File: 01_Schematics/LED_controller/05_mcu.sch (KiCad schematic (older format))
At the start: 28 parts, among them J48 PLS-4, U8 STM32F107RCTx, Y1 25 MHz

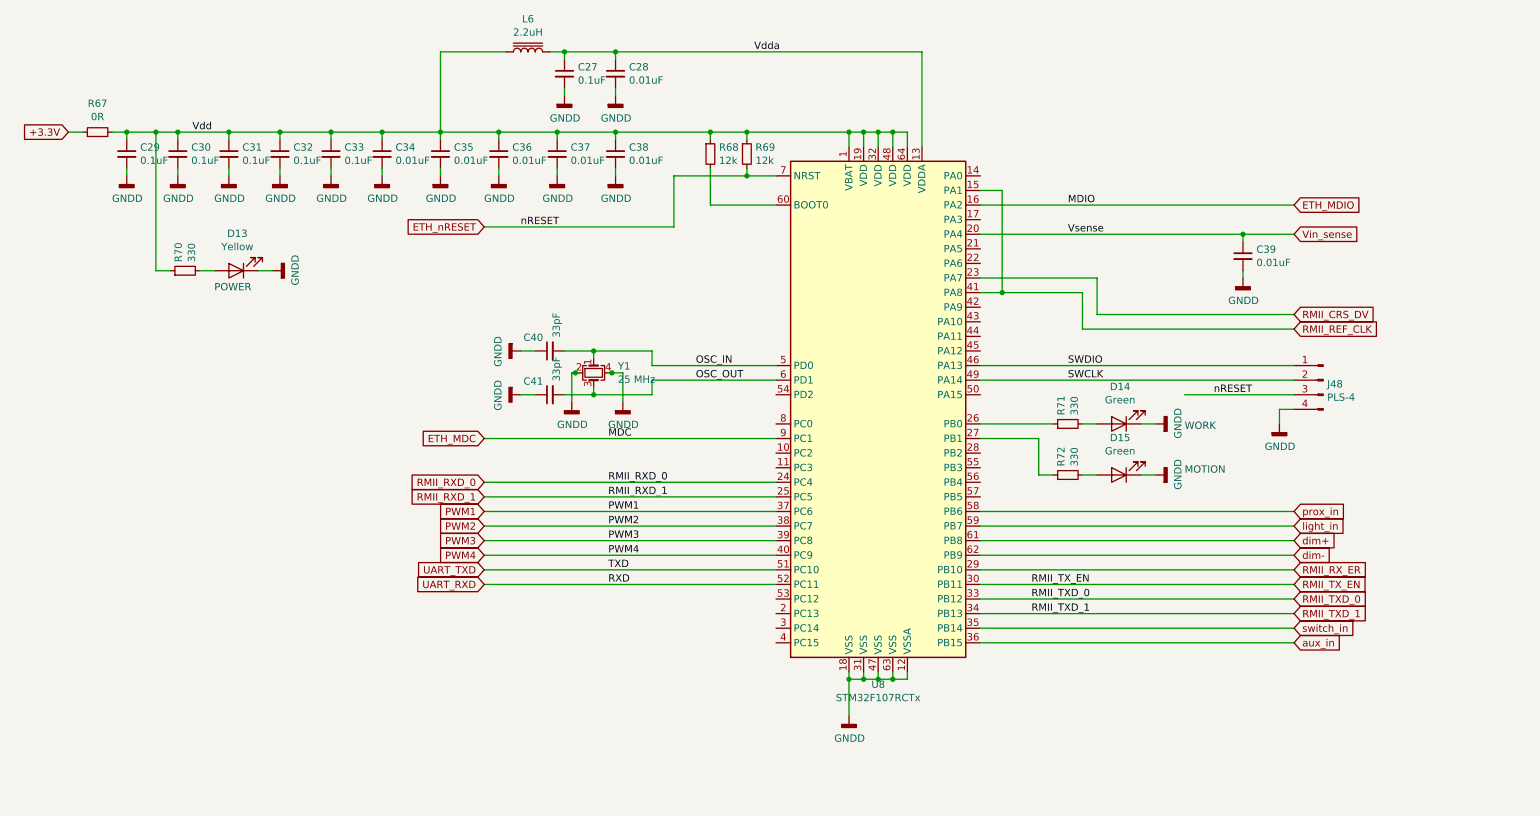
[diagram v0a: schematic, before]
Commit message: - Добавлена печатная плата; - Добавлены файлы посадочных мест использованных компонентов и STEP модели; - Добавлены файлы механической сборки (Solidworks);
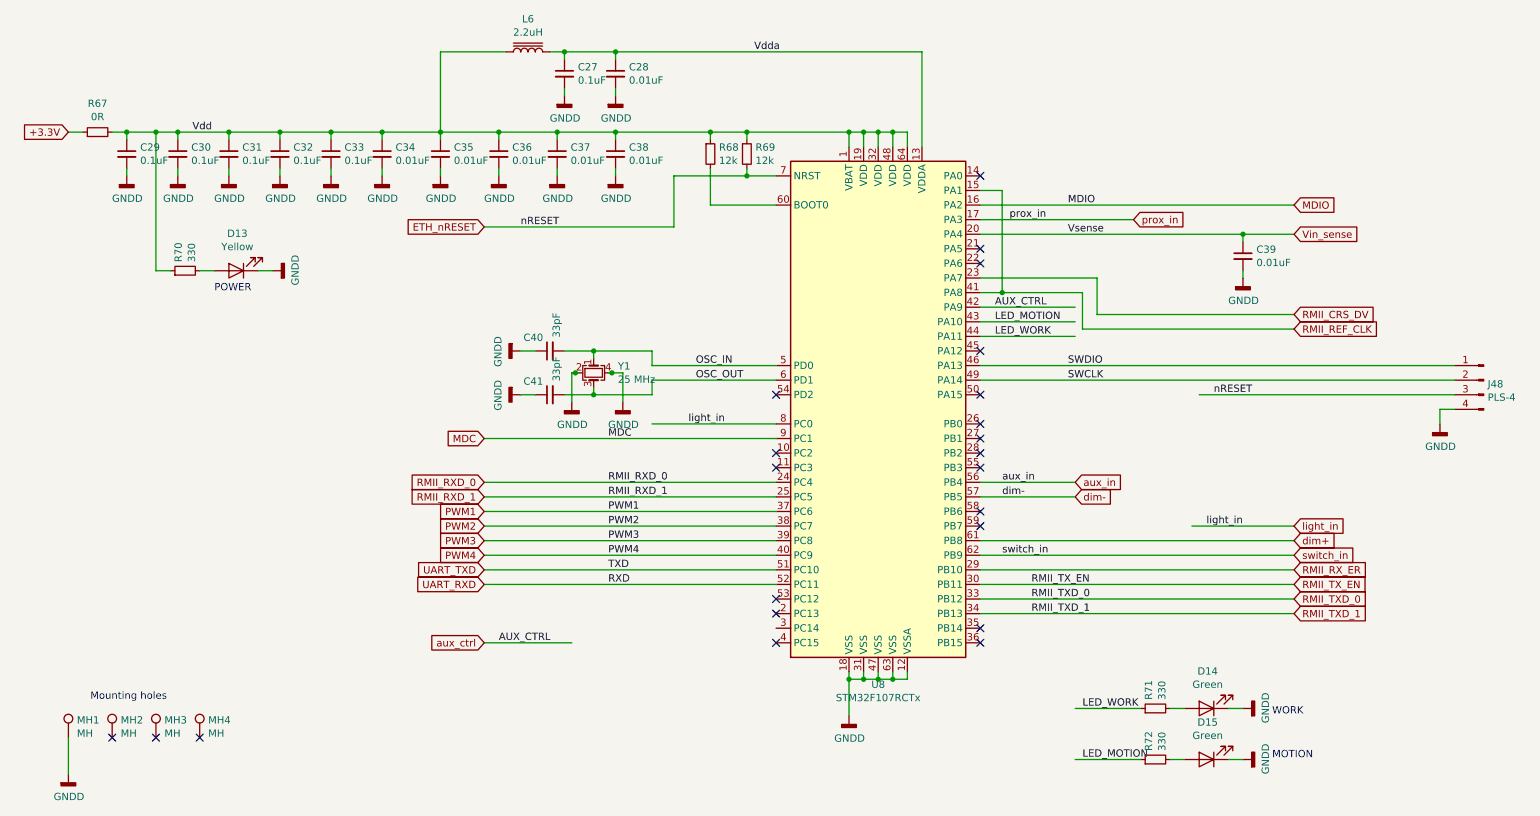
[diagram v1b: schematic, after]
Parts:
- added MH1, MH2, MH3, MH4: MH, MountingHole:MountingHole_3.2mm_M3_Pad_Via, symbol Connector:TestPoint
- D13, D14, D15: footprint Resistor_SMD:R_0805_2012Metric_Pad1.15x1.40mm_HandSolder -> extras:LED_0805_2012Metric_HandSolder
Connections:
- net labels added: AUX_CTRL, LED_MOTION, LED_WORK, aux_ctrl
- net labels removed: ETH_MDC, ETH_MDIO
- wire segments 141 -> 145
- no-connect marks 0 -> 22
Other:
- note added: "Mounting holes"
- moved on the sheet: D14, D15, J48, R71, R72

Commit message: - Исправлена ошибка с неправильным подключением цепи обратной связи микросхемы U1; - Плата переразведена с учетом изменений в схеме; - Добавлен файл BOM;
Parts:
- U8: partnum (none) -> STM32F107RCTx
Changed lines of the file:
@@
 F 2 "Package_QFP:LQFP-64_10x10mm_P0.5mm" H 5850 1600 50  0001 R CNN
 F 3 "http://www.st.com/st-web-ui/static/active/en/resource/technical/document/datasheet/CD00220364.pdf" H 6450 3300 50  0001 C CNN
+F 4 "STM32F107RCTx" H 6450 3300 50  0001 C CNN "partnum"
 	1    6450 3300
 	1    0    0    -1
